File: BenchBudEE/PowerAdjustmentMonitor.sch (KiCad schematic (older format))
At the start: 15 parts, among them U6 LM317, U7 LM317, U8 7805, U9 7805

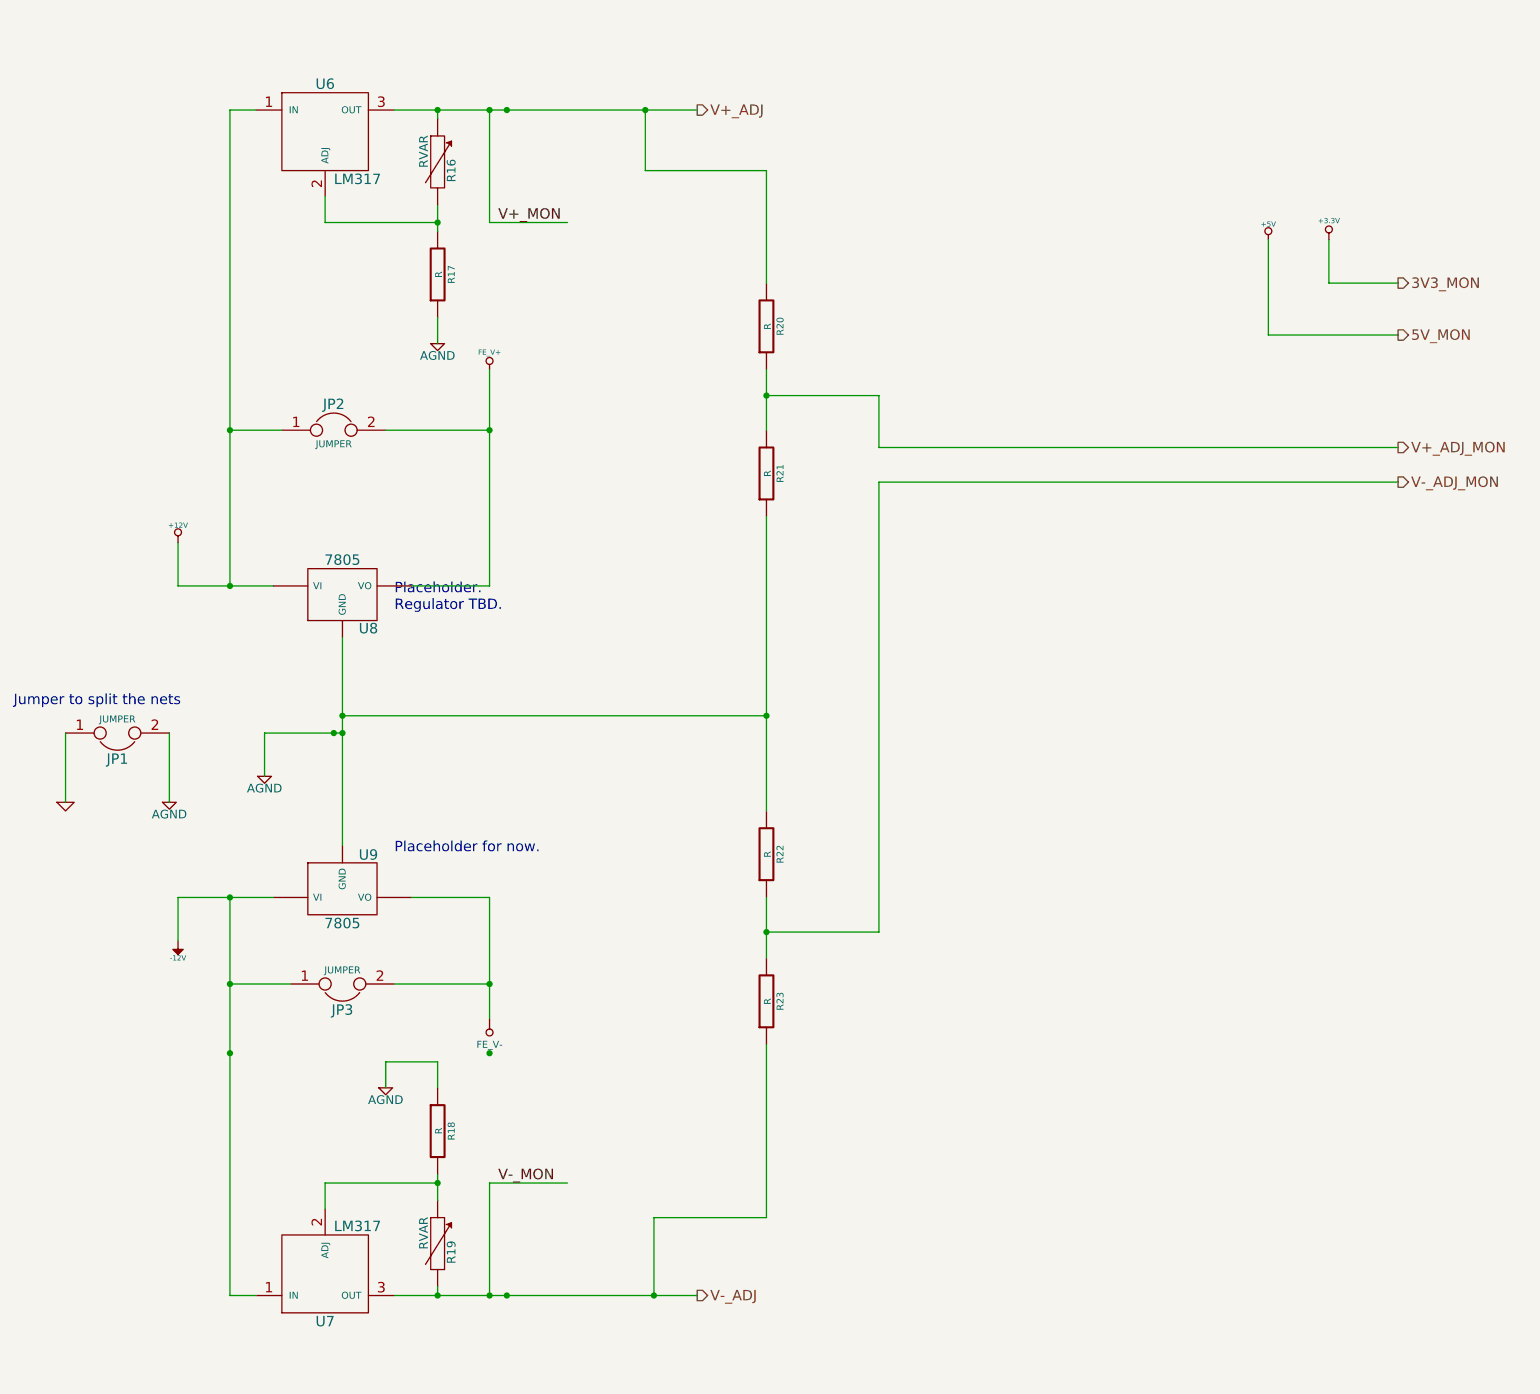
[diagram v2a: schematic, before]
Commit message: Associated the power modification module components.
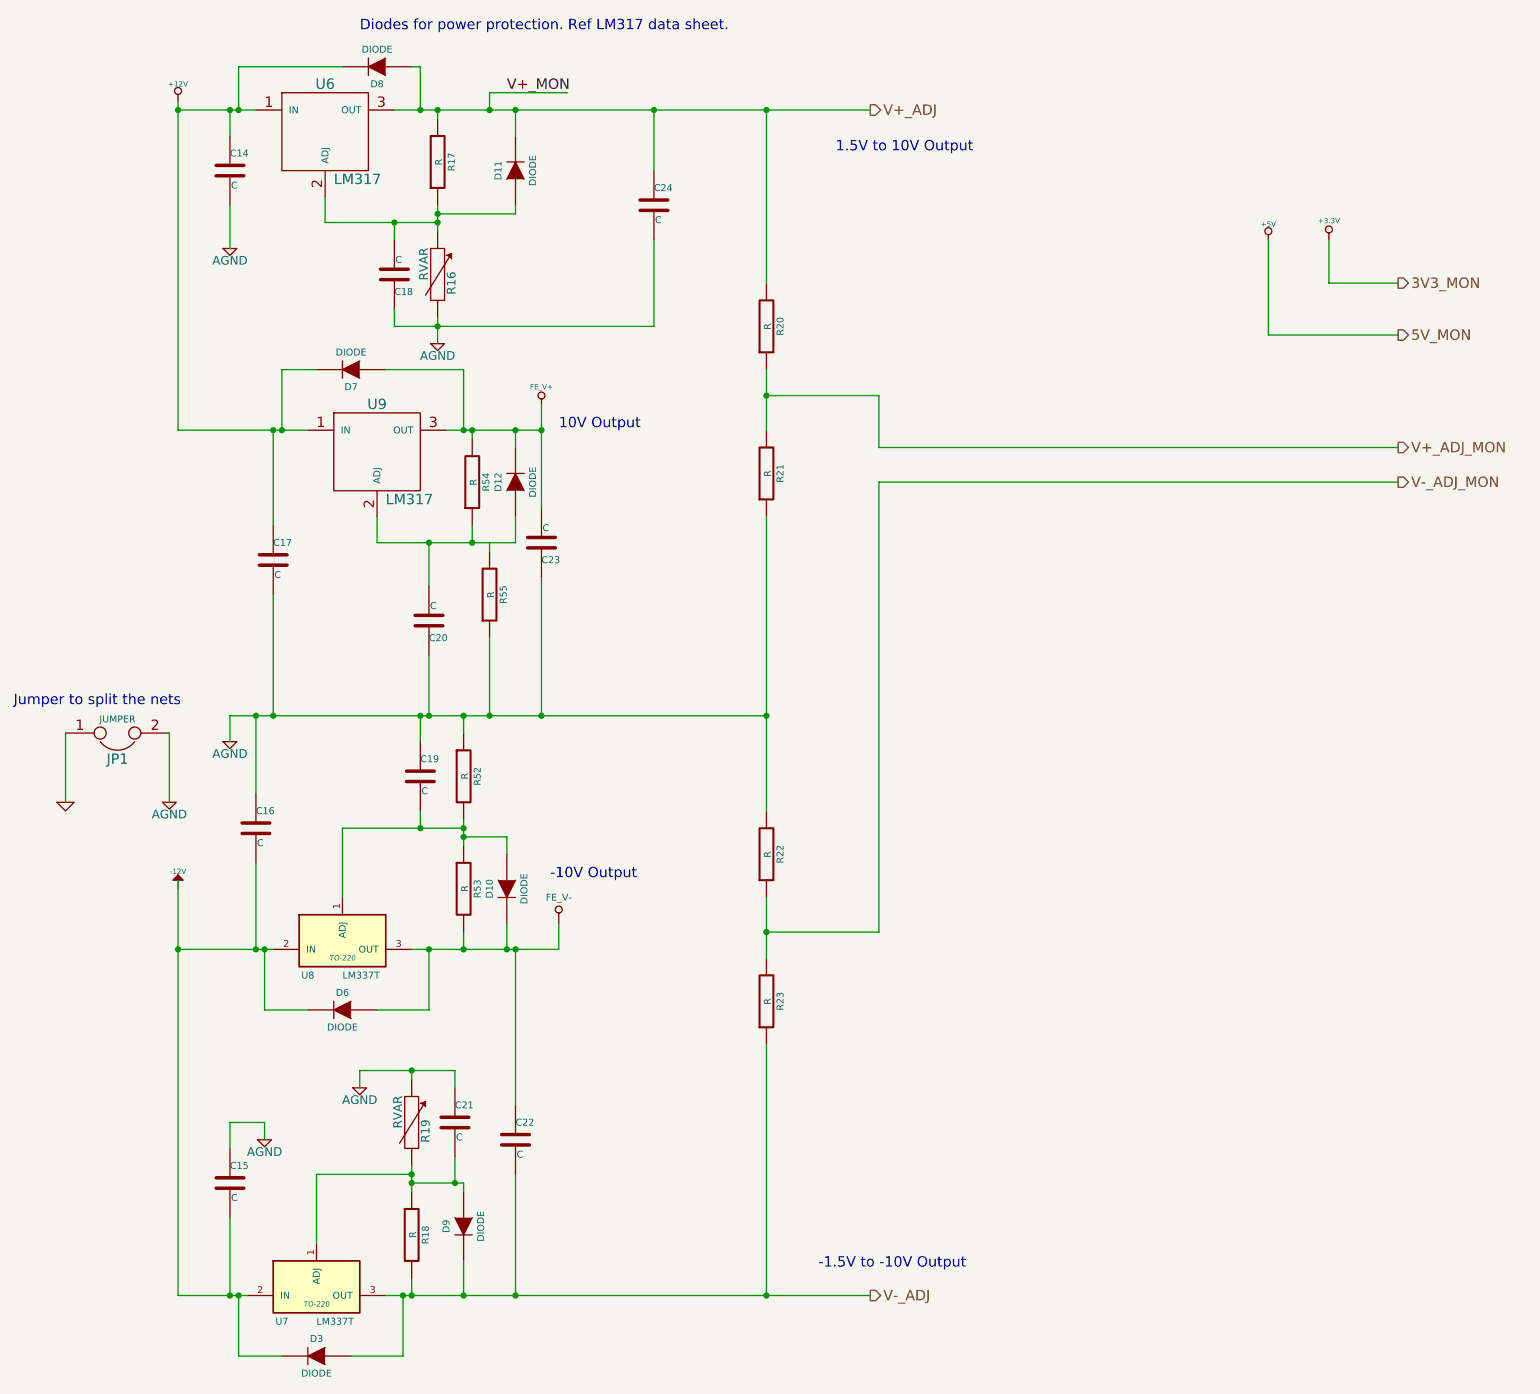
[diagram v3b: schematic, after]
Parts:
- removed JP2, JP3: JUMPER, ~, symbol JUMPER
- removed U7: LM317, ~, symbol LM317
- removed U8, U9: 7805, ~, symbol 7805
- added C14, C15, C16, C17, C18, C19, C20, C21, C22, C23, C24: C, ~, symbol C
- added D10, D11, D12, D3, D6, D7, D8, D9: DIODE, ~, symbol DIODE
- added R52, R53, R54, R55: R, ~, symbol R
- added U7, U8: LM337T, TO-220, symbol LM337T
- added U9: LM317, ~, symbol LM317
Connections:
- net labels removed: V-_MON
- wire segments 59 -> 107
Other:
- note added: "-1.5V to -10V Output"
- note added: "-10V Output"
- note added: "1.5V to 10V Output"
- note added: "10V Output"
- note added: "Diodes for power protection. Ref LM317 data sheet."
- note removed: "Placeholder for now."
- note removed: "Placeholder.\nRegulator TBD."
- moved on the sheet: R16, R17

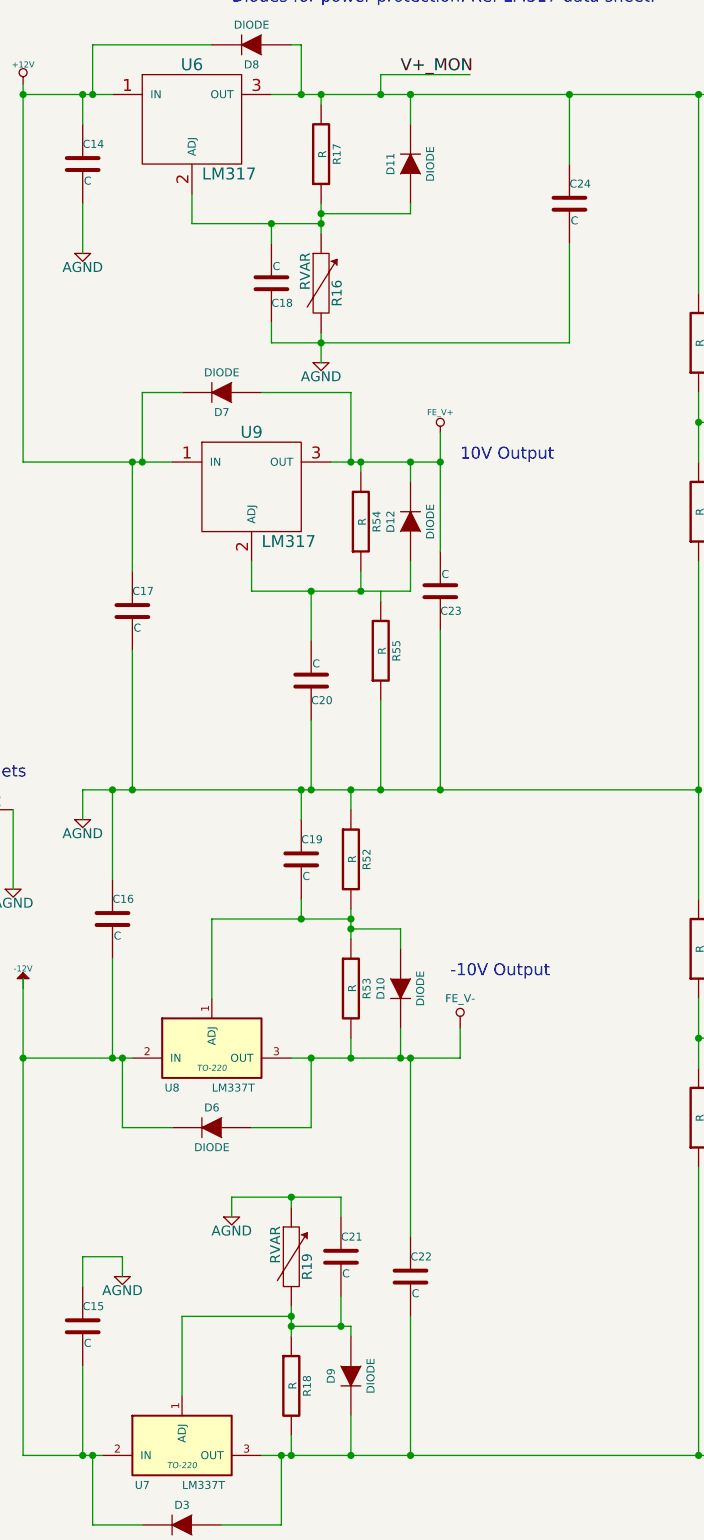
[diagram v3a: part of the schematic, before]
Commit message: Roughly placed the power modification module components.
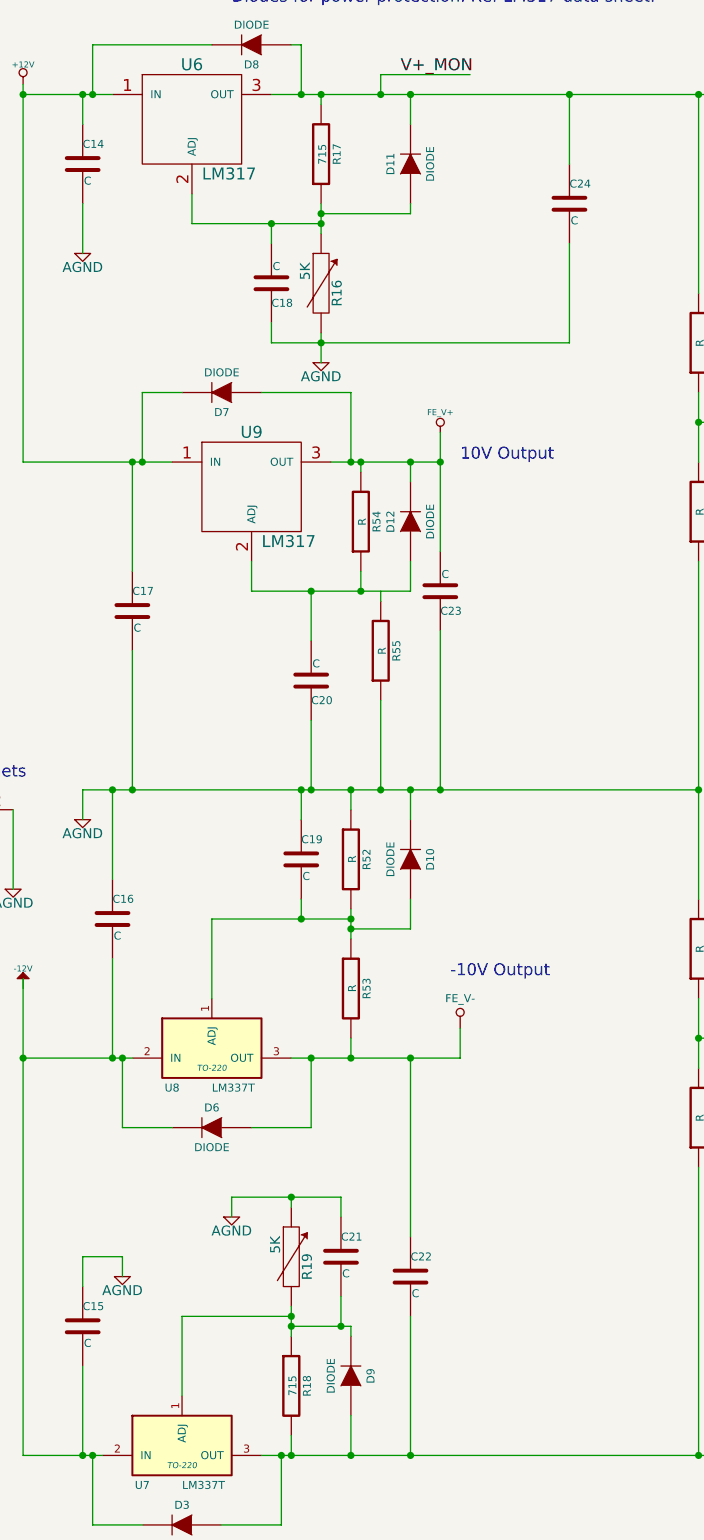
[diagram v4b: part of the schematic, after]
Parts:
- R16, R19: value RVAR -> 5K
- R17, R18: value R -> 715
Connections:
- net AGND: now also D10.2 (K)
- net FE_V-: no longer D10.2 (K)
- net V-_ADJ: now also D9.1 (A); no longer D9.2 (K)
- net at C21.2, R18.1, R19.2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: now also D9.2 (K); no longer D9.1 (A)
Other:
- moved on the sheet: D10
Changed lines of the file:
@@
 $EndDescr
 $Comp
-L +12V #PWR42
+L +12V #PWR038
 U 1 1 52F6DADC
 P 1450 700
-F 0 "#PWR42" H 1450 650 20  0001 C CNN
+F 0 "#PWR038" H 1450 650 20  0001 C CNN
 F 1 "+12V" H 1450 800 30  0000 C CNN
 F 2 "" H 1450 700 60  0000 C CNN
@@
 $EndComp
 $Comp
-L -12V #PWR43
+L -12V #PWR039
 U 1 1 52F6DAE4
 P 1450 5250
-F 0 "#PWR43" H 1450 5380 20  0001 C CNN
+F 0 "#PWR039" H 1450 5380 20  0001 C CNN
 F 1 "-12V" H 1450 5350 30  0000 C CNN
 F 2 "" H 1450 5250 60  0000 C CNN
@@
 $EndComp
 $Comp
-L +5V #PWR51
+L +5V #PWR040
 U 1 1 52F6DB6E
 P 7750 1500
-F 0 "#PWR51" H 7750 1590 20  0001 C CNN
+F 0 "#PWR040" H 7750 1590 20  0001 C CNN
 F 1 "+5V" H 7750 1590 30  0000 C CNN
 F 2 "" H 7750 1500 60  0000 C CNN
@@
 $EndComp
 $Comp
-L +3.3V #PWR52
+L +3.3V #PWR041
 U 1 1 52F6DB74
 P 8100 1500
-F 0 "#PWR52" H 8100 1460 30  0001 C CNN
+F 0 "#PWR041" H 8100 1460 30  0001 C CNN
 F 1 "+3.3V" H 8100 1610 30  0000 C CNN
 F 2 "" H 8100 1500 60  0000 C CNN
@@
 $EndComp
 $Comp
-L GND #PWR40
+L GND #PWR042
 U 1 1 52F72349
 P 800 4750
-F 0 "#PWR40" H 800 4750 30  0001 C CNN
+F 0 "#PWR042" H 800 4750 30  0001 C CNN
 F 1 "GND" H 800 4680 30  0001 C CNN
 F 2 "" H 800 4750 60  0000 C CNN
@@
 $EndComp
 $Comp
-L AGND #PWR41
+L AGND #PWR043
 U 1 1 52F726D0
 P 1400 4750
-F 0 "#PWR41" H 1400 4750 40  0001 C CNN
+F 0 "#PWR043" H 1400 4750 40  0001 C CNN
 F 1 "AGND" H 1400 4680 50  0000 C CNN
 F 2 "" H 1400 4750 60  0000 C CNN
@@
 $EndComp
 $Comp
-L AGND #PWR45
+L AGND #PWR044
 U 1 1 52F72728
 P 1750 4400
-F 0 "#PWR45" H 1750 4400 40  0001 C CNN
+F 0 "#PWR044" H 1750 4400 40  0001 C CNN
 F 1 "AGND" H 1750 4330 50  0000 C CNN
 F 2 "" H 1750 4400 60  0000 C CNN
@@
 Jumper to split the nets
 $Comp
-L FE_V+ #PWR49
+L FE_V+ #PWR045
 U 1 1 52F72F13
 P 3550 2450
-F 0 "#PWR49" H 3550 2550 30  0001 C CNN
+F 0 "#PWR045" H 3550 2550 30  0001 C CNN
 F 1 "FE_V+" H 3550 2550 30  0000 C CNN
 F 2 "" H 3550 2450 60  0000 C CNN
@@
 P 2950 1050
 F 0 "R17" V 3030 1050 40  0000 C CNN
-F 1 "R" V 2957 1051 40  0000 C CNN
+F 1 "715" V 2957 1051 40  0000 C CNN
 F 2 "~" V 2880 1050 30  0000 C CNN
 F 3 "~" H 2950 1050 30  0000 C CNN
@@
 Connection ~ 2950 1400
 $Comp
-L AGND #PWR48
+L AGND #PWR046
 U 1 1 52F73CA7
 P 2950 2100
-F 0 "#PWR48" H 2950 2100 40  0001 C CNN
+F 0 "#PWR046" H 2950 2100 40  0001 C CNN
 F 1 "AGND" H 2950 2030 50  0000 C CNN
 F 2 "" H 2950 2100 60  0000 C CNN
@@
 P 2950 1700
 F 0 "R16" V 3030 1650 50  0000 C CNN
-F 1 "RVAR" V 2870 1760 50  0000 C CNN
+F 1 "5K" V 2870 1760 50  0000 C CNN
 F 2 "~" H 2950 1700 60  0000 C CNN
 F 3 "~" H 2950 1700 60  0000 C CNN
@@
 P 2800 7250
 F 0 "R18" V 2880 7250 40  0000 C CNN
-F 1 "R" V 2807 7251 40  0000 C CNN
+F 1 "715" V 2807 7251 40  0000 C CNN
 F 2 "~" V 2730 7250 30  0000 C CNN
 F 3 "~" H 2800 7250 30  0000 C CNN
@@
 	2800 7600 2800 7500
 $Comp
-L AGND #PWR47
+L AGND #PWR047
 U 1 1 530959E2
 P 2500 6400
-F 0 "#PWR47" H 2500 6400 40  0001 C CNN
+F 0 "#PWR047" H 2500 6400 40  0001 C CNN
 F 1 "AGND" H 2500 6330 50  0000 C CNN
 F 2 "" H 2500 6400 60  0000 C CNN
@@
 P 2800 6600
 F 0 "R19" V 2880 6550 50  0000 C CNN
-F 1 "RVAR" V 2720 6660 50  0000 C CNN
+F 1 "5K" V 2720 6660 50  0000 C CNN
 F 2 "~" H 2800 6600 60  0000 C CNN
 F 3 "~" H 2800 6600 60  0000 C CNN
@@
 $EndComp
 $Comp
-L AGND #PWR44
+L AGND #PWR048
 U 1 1 530992E8
 P 1750 1550
-F 0 "#PWR44" H 1750 1550 40  0001 C CNN
+F 0 "#PWR048" H 1750 1550 40  0001 C CNN
 F 1 "AGND" H 1750 1480 50  0000 C CNN
 F 2 "" H 1750 1550 60  0000 C CNN
@@
 	1750 1550 1750 1300
 $Comp
-L AGND #PWR46
+L AGND #PWR049
 U 1 1 530993D8
 P 1950 6700
-F 0 "#PWR46" H 1950 6700 40  0001 C CNN
+F 0 "#PWR049" H 1950 6700 40  0001 C CNN
 F 1 "AGND" H 1950 6630 50  0000 C CNN
 F 2 "" H 1950 6700 60  0000 C CNN
@@
 L DIODE D10
 U 1 1 5309B49F
-P 3350 5250
-F 0 "D10" H 3350 5350 40  0000 C CNN
-F 1 "DIODE" H 3350 5150 40  0000 C CNN
-F 2 "~" H 3350 5250 60  0000 C CNN
-F 3 "~" H 3350 5250 60  0000 C CNN
-	1    3350 5250
-	0    -1   1    0
-$EndComp
-Wire Wire Line
-	3100 4950 3350 4950
-Wire Wire Line
-	3350 4950 3350 5050
+P 3400 4600
+F 0 "D10" H 3400 4700 40  0000 C CNN
+F 1 "DIODE" H 3400 4500 40  0000 C CNN
+F 2 "~" H 3400 4600 60  0000 C CNN
+F 3 "~" H 3400 4600 60  0000 C CNN
+	1    3400 4600
+	0    1    -1   0
+$EndComp
+Wire Wire Line
+	3100 4950 3400 4950
 Connection ~ 3100 4950
-Wire Wire Line
-	3350 5450 3350 5600
-Connection ~ 3350 5600
 $Comp
 L DIODE D6
@@
 F 3 "~" H 3100 7200 60  0000 C CNN
 	1    3100 7200
-	0    -1   1    0
+	0    1    -1   0
 $EndComp
 Wire Wire Line
@@
 Text Notes 2500 300  0    60   ~ 0
 Diodes for power protection. Ref LM317 data sheet.
+Wire Wire Line
+	3400 4950 3400 4800
+Wire Wire Line
+	3400 4400 3400 4250
+Connection ~ 3400 4250
 $EndSCHEMATC
